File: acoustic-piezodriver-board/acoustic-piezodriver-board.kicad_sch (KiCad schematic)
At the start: 5 parts, among them P101 WJ128V-5.0-3P, U101 AMS1117-3.3, U102 TMCS1108A3UQDR

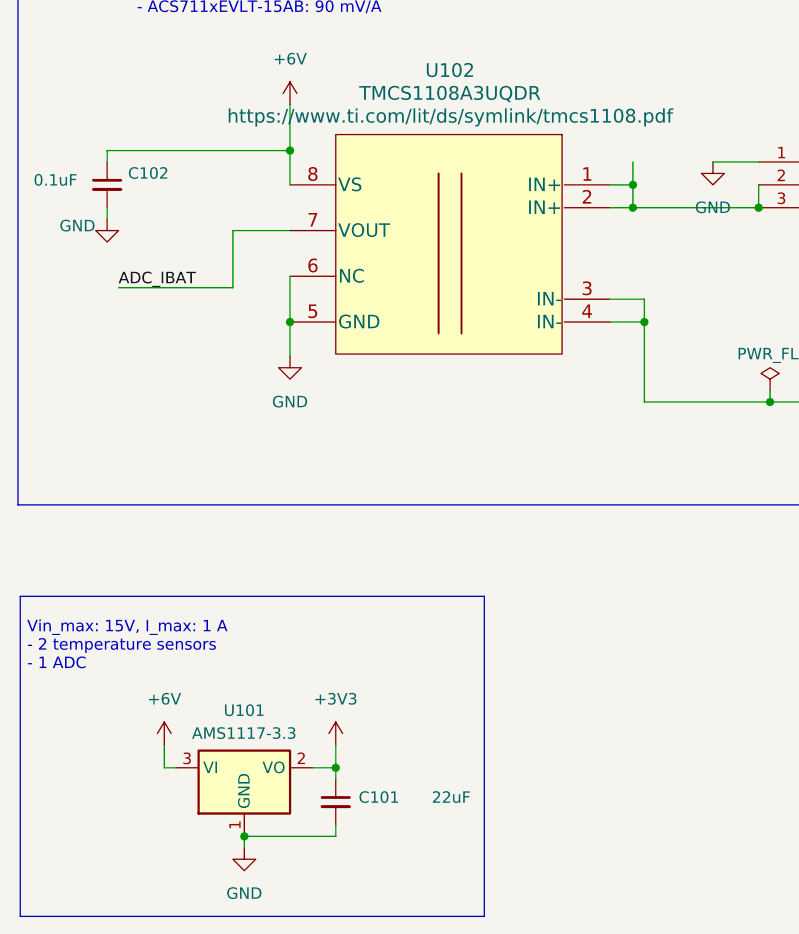
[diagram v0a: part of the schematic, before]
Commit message: Fixed ERC, DRC errors, finished routing (next) perform footprint checks
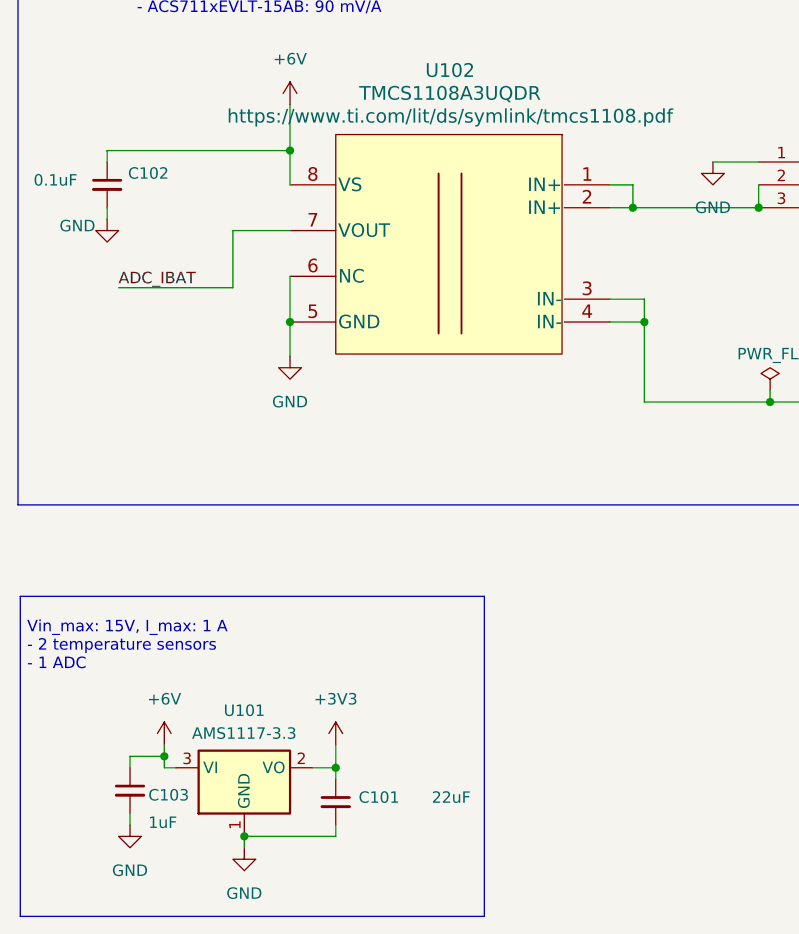
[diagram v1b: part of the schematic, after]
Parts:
- added C103: 1uF, Capacitor_SMD:C_0805_2012Metric, symbol Device:C_Small
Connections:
- net +6V: now also C103.1
- net GND: now also C103.2
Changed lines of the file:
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@@
+	)
+	(junction
+		(at 34.29 146.05)
+		(diameter 0)
+		(color 0 0 0 0)
 	)
 	(junction
@@
 	)
 	(junction
-		(at 86.36 82.55)
-		(diameter 0)
-		(color 0 0 0 0)
-	)
-	(junction
 		(at 101.6 106.68)
 		(diameter 0)
@@
 	(wire
 		(pts
-			(xy 34.29 144.78) (xy 34.29 147.32)
+			(xy 34.29 144.78) (xy 34.29 146.05)
 		)
 		(stroke
@@
 	(wire
 		(pts
+			(xy 30.48 146.05) (xy 34.29 146.05)
+		)
+		(stroke
+			(width 0)
+			(type default)
+		)
+	)
+	(wire
+		(pts
 			(xy 203.2 66.04) (xy 214.63 66.04)
 		)
@@
 	(wire
 		(pts
+			(xy 30.48 147.32) (xy 30.48 146.05)
+		)
+		(stroke
+			(width 0)
+			(type default)
+		)
+	)
+	(wire
+		(pts
 			(xy 86.36 85.09) (xy 86.36 82.55)
 		)
@@
 	(wire
 		(pts
+			(xy 34.29 146.05) (xy 34.29 147.32)
+		)
+		(stroke
+			(width 0)
+			(type default)
+		)
+	)
+	(wire
+		(pts
 			(xy 241.3 76.2) (xy 241.3 99.06)
 		)
@@
 	(wire
 		(pts
+			(xy 30.48 152.4) (xy 30.48 153.67)
+		)
+		(stroke
+			(width 0)
+			(type default)
+		)
+	)
+	(wire
+		(pts
 			(xy 83.82 97.79) (xy 87.63 97.79)
-		)
-		(stroke
-			(width 0)
-			(type default)
-		)
-	)
-	(wire
-		(pts
-			(xy 86.36 80.01) (xy 86.36 82.55)
 		)
 		(stroke
@@
 			)
 			(justify right bottom)
+		)
+	)
+	(symbol
+		(lib_id "Device:C_Small")
+		(at 30.48 149.86 0)
+		(unit 1)
+		(exclude_from_sim no)
+		(in_bom yes)
+		(on_board yes)
+		(dnp no)
+		(property "Reference" "C103"
+			(at 32.512 150.368 0)
+			(effects
+				(font
+					(size 1.27 1.27)
+				)
+				(justify left)
+			)
+		)
+		(property "Value" "1uF"
+			(at 32.512 153.416 0)
+			(effects
+				(font
+					(size 1.27 1.27)
+				)
+				(justify left)
+			)
+		)
+		(property "Footprint" "Capacitor_SMD:C_0805_2012Metric"
+			(at 30.48 149.86 0)
+			(effects
+				(font
+					(size 1.27 1.27)
+				)
+				(hide yes)
+			)
+		)
+		(property "Datasheet" "~"
+			(at 30.48 149.86 0)
+			(effects
+				(font
+					(size 1.27 1.27)
+				)
+				(hide yes)
+			)
+		)
+		(property "Description" "Unpolarized capacitor, small symbol"
+			(at 30.48 149.86 0)
+			(effects
+				(font
+					(size 1.27 1.27)
+				)
+				(hide yes)
+			)
+		)
+		(property "Manufacturing Part Number" "CL21B105KBFNNNE"
+			(at 30.48 149.86 0)
+			(effects
+				(font
+					(size 1.27 1.27)
+				)
+				(hide yes)
+			)
+		)
+		(property "LCSC Part Number" "C28323"
+			(at 30.48 149.86 0)
+			(effects
+				(font
+					(size 1.27 1.27)
+				)
+				(hide yes)
+			)
+		)
+		(pin "1"
+		)
+		(pin "2"
+		)
+		(instances
+			(project "acoustic-piezodriver-board"
+				(path "/94cb090f-214e-44cc-b8ed-ae50ff29d2bf"
+					(reference "C103")
+					(unit 1)
+				)
+			)
 		)
 	)
@@
 					(unit 1)
 				)
+			)
+		)
+	)
+	(symbol
+		(lib_id "power:GND")
+		(at 30.48 153.67 0)
+		(unit 1)
+		(exclude_from_sim no)
+		(in_bom yes)
+		(on_board yes)
+		(dnp no)
+		(fields_autoplaced yes)
+		(property "Reference" "#PWR0108"
+			(at 30.48 160.02 0)
+			(effects
+				(font
+					(size 1.27 1.27)
+				)
+				(hide yes)
+			)
+		)
+		(property "Value" "GND"
+			(at 30.48 158.75 0)
+			(effects
+				(font
+					(size 1.27 1.27)
+				)
+			)
+		)
+		(property "Footprint" ""
+			(at 30.48 153.67 0)
+			(effects
+				(font
+					(size 1.27 1.27)
+				)
+				(hide yes)
+			)
+		)
+		(property "Datasheet" ""
+			(at 30.48 153.67 0)
+			(effects
+				(font
+					(size 1.27 1.27)
+				)
+				(hide yes)
+			)
+		)
+		(property "Description" "Power symbol creates a global label with name \"GND\" , ground"
+			(at 30.48 153.67 0)
+			(effects
+				(font
+					(size 1.27 1.27)
+				)
+				(hide yes)
+			)
+		)
+		(pin "1"
+		)
+		(instances
+			(project "acoustic-piezodriver-board"
+				(path "/94cb090f-214e-44cc-b8ed-ae50ff29d2bf"
+					(reference "#PWR0108")
+					(unit 1)
+				)

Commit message: [production checks] checked caps, [todo] Think about replacing 220 nF filtering caps in DC-DC to 0402 package (next) check rest of footprints
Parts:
- C103: LCSC Part Number C28323 -> (none); LPN (none) -> C28323; MPN (none) -> CL21B105KBFNNNE; Manufacturing Part Number CL21B105KBFNNNE -> (none)
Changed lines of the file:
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@@
 			)
 		)
-		(property "Manufacturing Part Number" "CL21B105KBFNNNE"
+		(property "LPN" "C28323"
 			(at 30.48 149.86 0)
 			(effects
@@
 			)
 		)
-		(property "LCSC Part Number" "C28323"
+		(property "MPN" "CL21B105KBFNNNE"
 			(at 30.48 149.86 0)
 			(effects

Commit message: added testpoints on fb and isense pins (next) double-check schematic and order
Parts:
- C101: LCSC Part Number (none) -> C45783; LPN C45783 -> (none); MPN CL21A226MAQNNNE -> (none); Manufacturing Part Number (none) -> CL21A226MAQNNNE
- C102: LCSC Part Number (none) -> C307331; LPN C307331 -> (none); MPN CL05B104KB54PNC -> (none); Manufacturing Part Number (none) -> CL05B104KB54PNC
- C103: LCSC Part Number (none) -> C28323; LPN C28323 -> (none); MPN CL21B105KBFNNNE -> (none); Manufacturing Part Number (none) -> CL21B105KBFNNNE
- P101: LCSC Part Number (none) -> C8270; LPN C8270 -> (none); MPN WJ128V-5.0-3P -> (none); Manufacturing Part Number (none) -> WJ128V-5.0-3P
- U101: LCSC Part Number (none) -> C6186; LPN C6186 -> (none); MPN AMS1117-3.3 -> (none); Manufacturing Part Number (none) -> AMS1117-3.3
- U102: LCSC Part Number (none) -> C3684263; LPN C3684263 -> (none); MPN TMCS1108A3UQDR -> (none); Manufacturing Part Number (none) -> TMCS1108A3UQDR
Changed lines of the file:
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@@
 			)
 		)
-		(property "LPN" "C28323"
+		(property "LCSC Part Number" "C28323"
 			(at 30.48 149.86 0)
 			(effects
@@
 			)
 		)
-		(property "MPN" "CL21B105KBFNNNE"
+		(property "Manufacturing Part Number" "CL21B105KBFNNNE"
 			(at 30.48 149.86 0)
 			(effects
@@
 			)
 		)
-		(property "LPN" "C3684263"
+		(property "LCSC Part Number" "C3684263"
 			(at 83.82 82.55 0)
 			(effects
@@
 			)
 		)
-		(property "MPN" "TMCS1108A3UQDR"
+		(property "Manufacturing Part Number" "TMCS1108A3UQDR"
 			(at 83.82 82.55 0)
 			(effects
@@
 			)
 		)
-		(property "LPN" "C8270"
-			(at 87.63 82.55 0)
-			(effects
-				(font
-					(size 1.27 1.27)
-				)
-				(hide yes)
-			)
-		)
-		(property "MPN" "WJ128V-5.0-3P "
+		(property "LCSC Part Number" "C8270"
+			(at 105.41 82.55 90)
+			(effects
+				(font
+					(size 1.27 1.27)
+				)
+				(hide yes)
+			)
+		)
+		(property "Manufacturing Part Number" "WJ128V-5.0-3P "
 			(at 105.41 82.55 90)
 			(effects
@@
 			)
 		)
-		(property "LPN" "C307331"
+		(property "LCSC Part Number" "C307331"
 			(at 27.94 82.55 0)
 			(effects
@@
 			)
 		)
-		(property "MPN" "CL05B104KB54PNC"
+		(property "Manufacturing Part Number" "CL05B104KB54PNC"
 			(at 27.94 82.55 0)
 			(effects
@@
 			)
 		)
-		(property "LPN" "C6186"
+		(property "LCSC Part Number" "C6186"
 			(at 43.18 147.32 0)
 			(effects
@@
 			)
 		)
-		(property "MPN" "AMS1117-3.3 "
+		(property "Manufacturing Part Number" "AMS1117-3.3 "
 			(at 43.18 147.32 0)
 			(effects
@@
 			)
 		)
-		(property "LPN" "C45783"
+		(property "LCSC Part Number" "C45783"
 			(at 53.34 151.13 0)
 			(effects
@@
 			)
 		)
-		(property "MPN" "CL21A226MAQNNNE"
+		(property "Manufacturing Part Number" "CL21A226MAQNNNE"
 			(at 53.34 151.13 0)
 			(effects

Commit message: added gerbers
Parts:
- added FID101, FID102, FID103, FID104: Fiducial, Fiducial:Fiducial_1mm_Mask2mm, symbol Mechanical:Fiducial
- added H101, H102, H103: MountingHole, MountingHole:ToolingHole_1.152mm, symbol Mechanical:MountingHole
